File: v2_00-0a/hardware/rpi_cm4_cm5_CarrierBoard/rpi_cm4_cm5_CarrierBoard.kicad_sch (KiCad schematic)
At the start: 5 parts

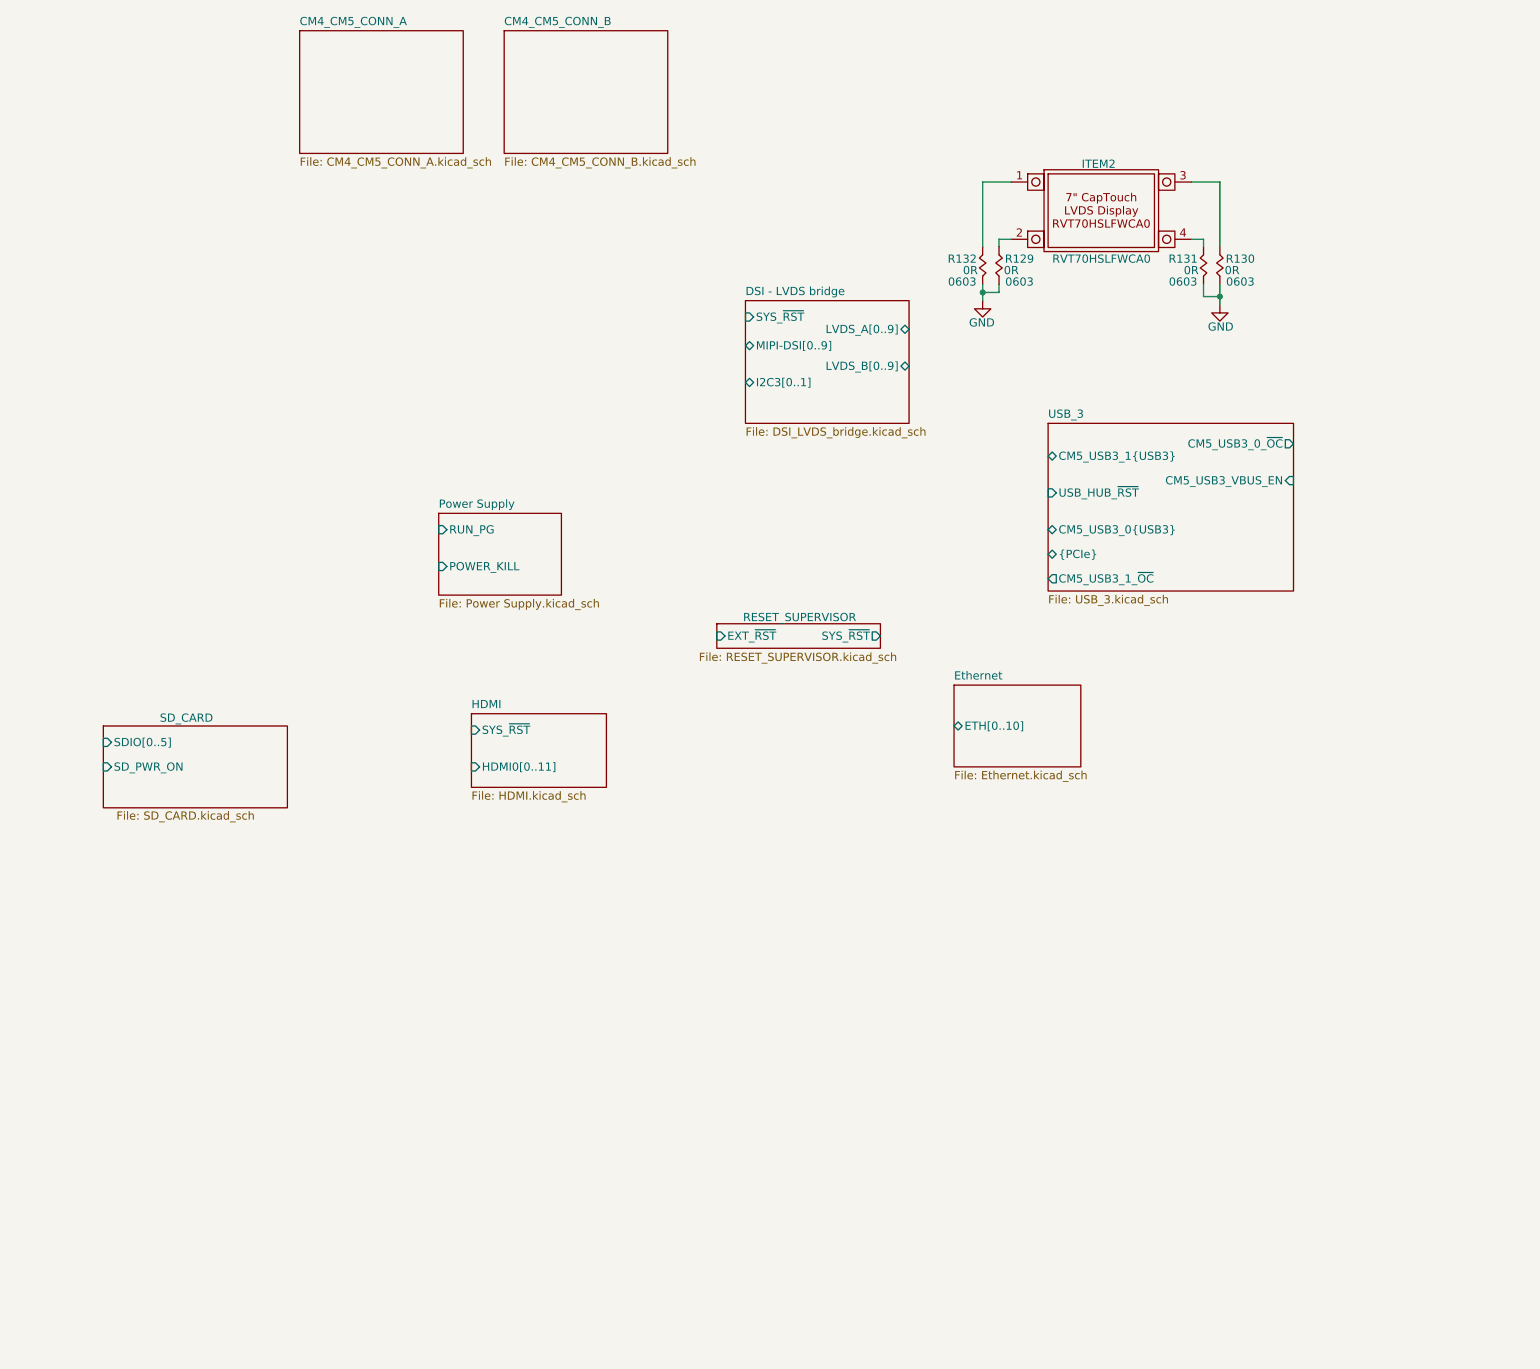
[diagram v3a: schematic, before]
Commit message: Add new page and update schematics
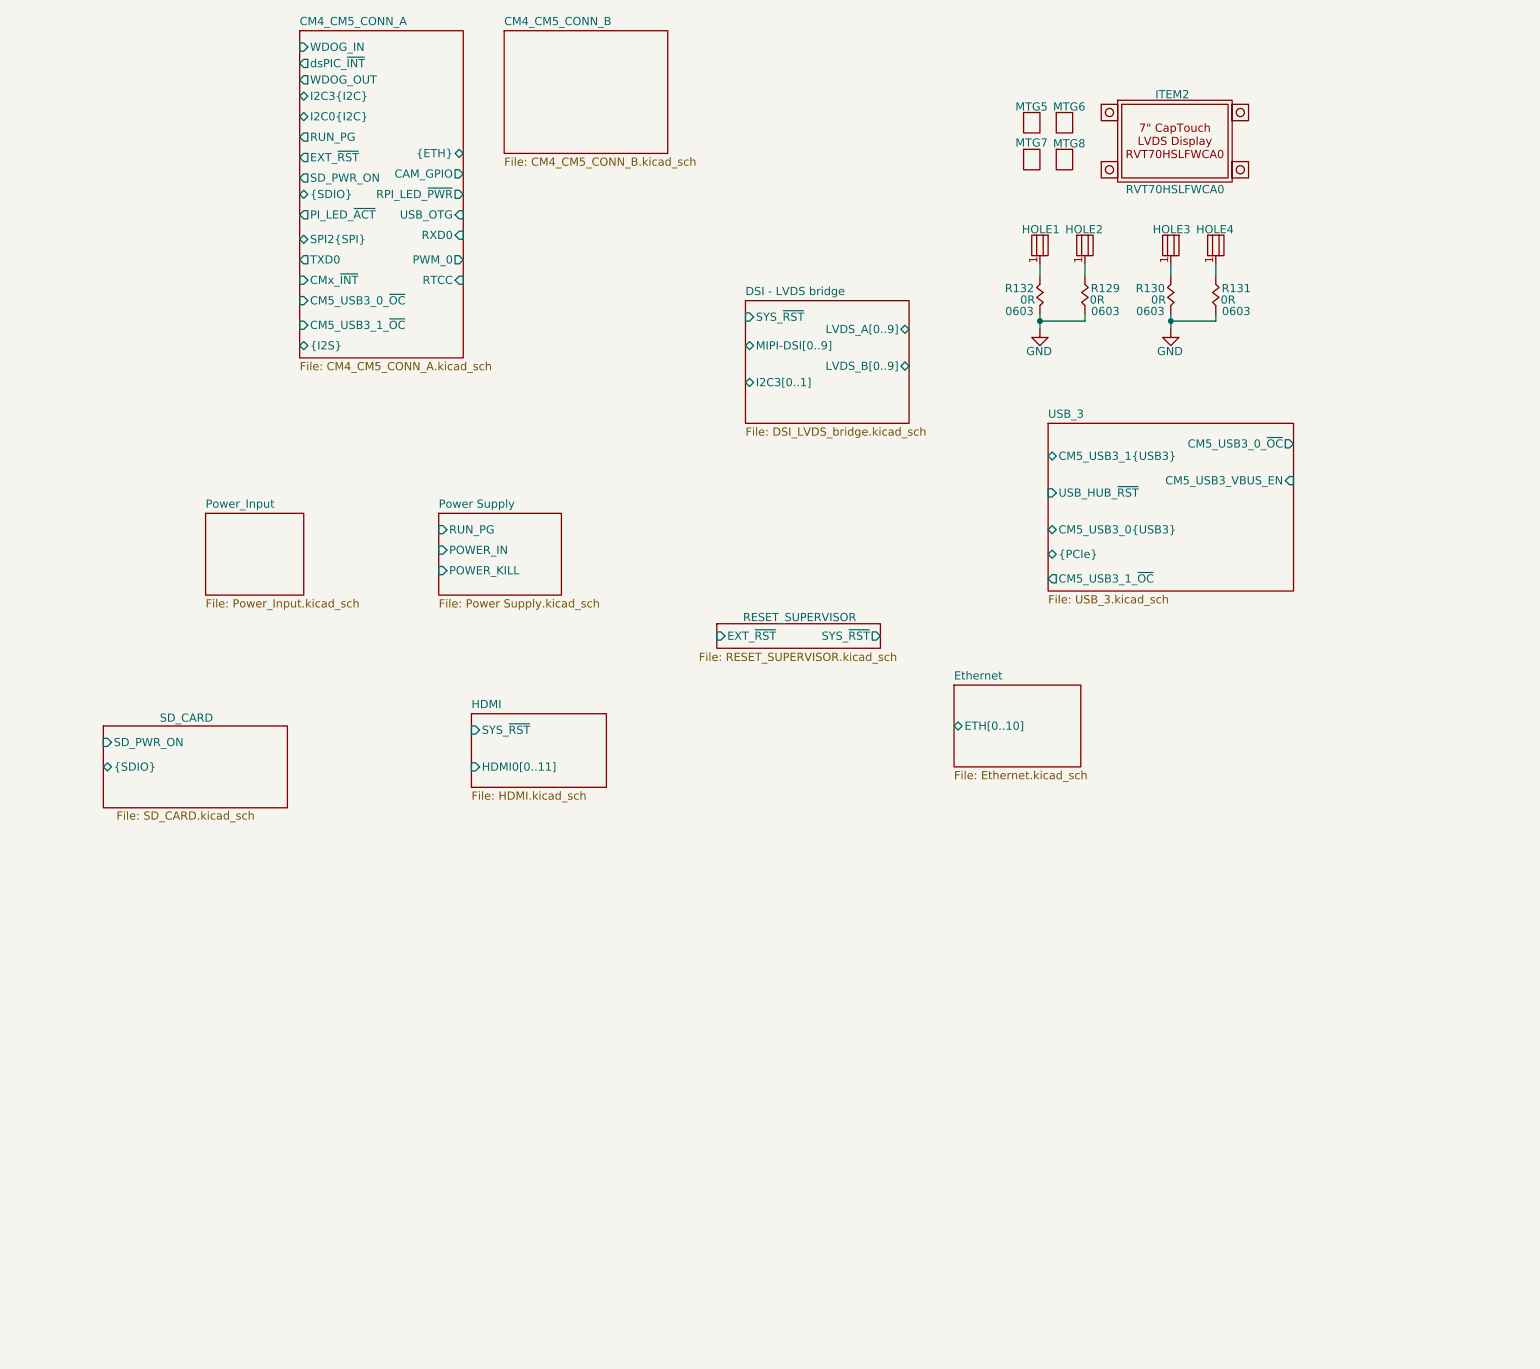
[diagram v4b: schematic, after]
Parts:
- added HOLE1, HOLE2, HOLE3, HOLE4: MTG_hole_cir_5mm_pad_3mm_drill, MTG_hole_cir_5mm_pad_3mm_drill, symbol KiCad_Lib_Symbols:MTG_hole_cir_5mm_pad_3mm_drill
- added MTG5, MTG6, MTG7, MTG8: M0504-25-AL-7, footprint:M0504-25-AL-7, symbol KicadCompDb:Miscellaneous/MISC_00004
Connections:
- net at R130.1: now also HOLE3.1; no longer ITEM2.3
- net at R132.1: now also HOLE1.1; no longer ITEM2.1
- net at R129.1: now also HOLE2.1; no longer ITEM2.2
- net at R131.1: now also HOLE4.1; no longer ITEM2.4
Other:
- added sheet Power_Input (Power_Input.kicad_sch)
- sheet CM4_CM5_CONN_A ports: added CAM_GPIO, CM5_USB3_0_~{OC}, CM5_USB3_1_~{OC}, CMx_~{INT}, EXT_~{RST}, I2C0{I2C}, I2C3{I2C}, PI_LED_~{ACT}, PWM_0, RPI_LED_~{PWR}, RTCC, RUN_PG, RXD0, SD_PWR_ON, SPI2{SPI}, TXD0, USB_OTG, WDOG_IN, WDOG_OUT, dsPIC_~{INT}, {ETH}, {I2S}, {SDIO}; removed none
- sheet Power Supply ports: added POWER_IN; removed none
- sheet SD_CARD ports: added {SDIO}; removed SDIO[0..5]
- moved on the sheet: R129, R132

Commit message: Add design notes (power table) and latest changes to power supply and power input
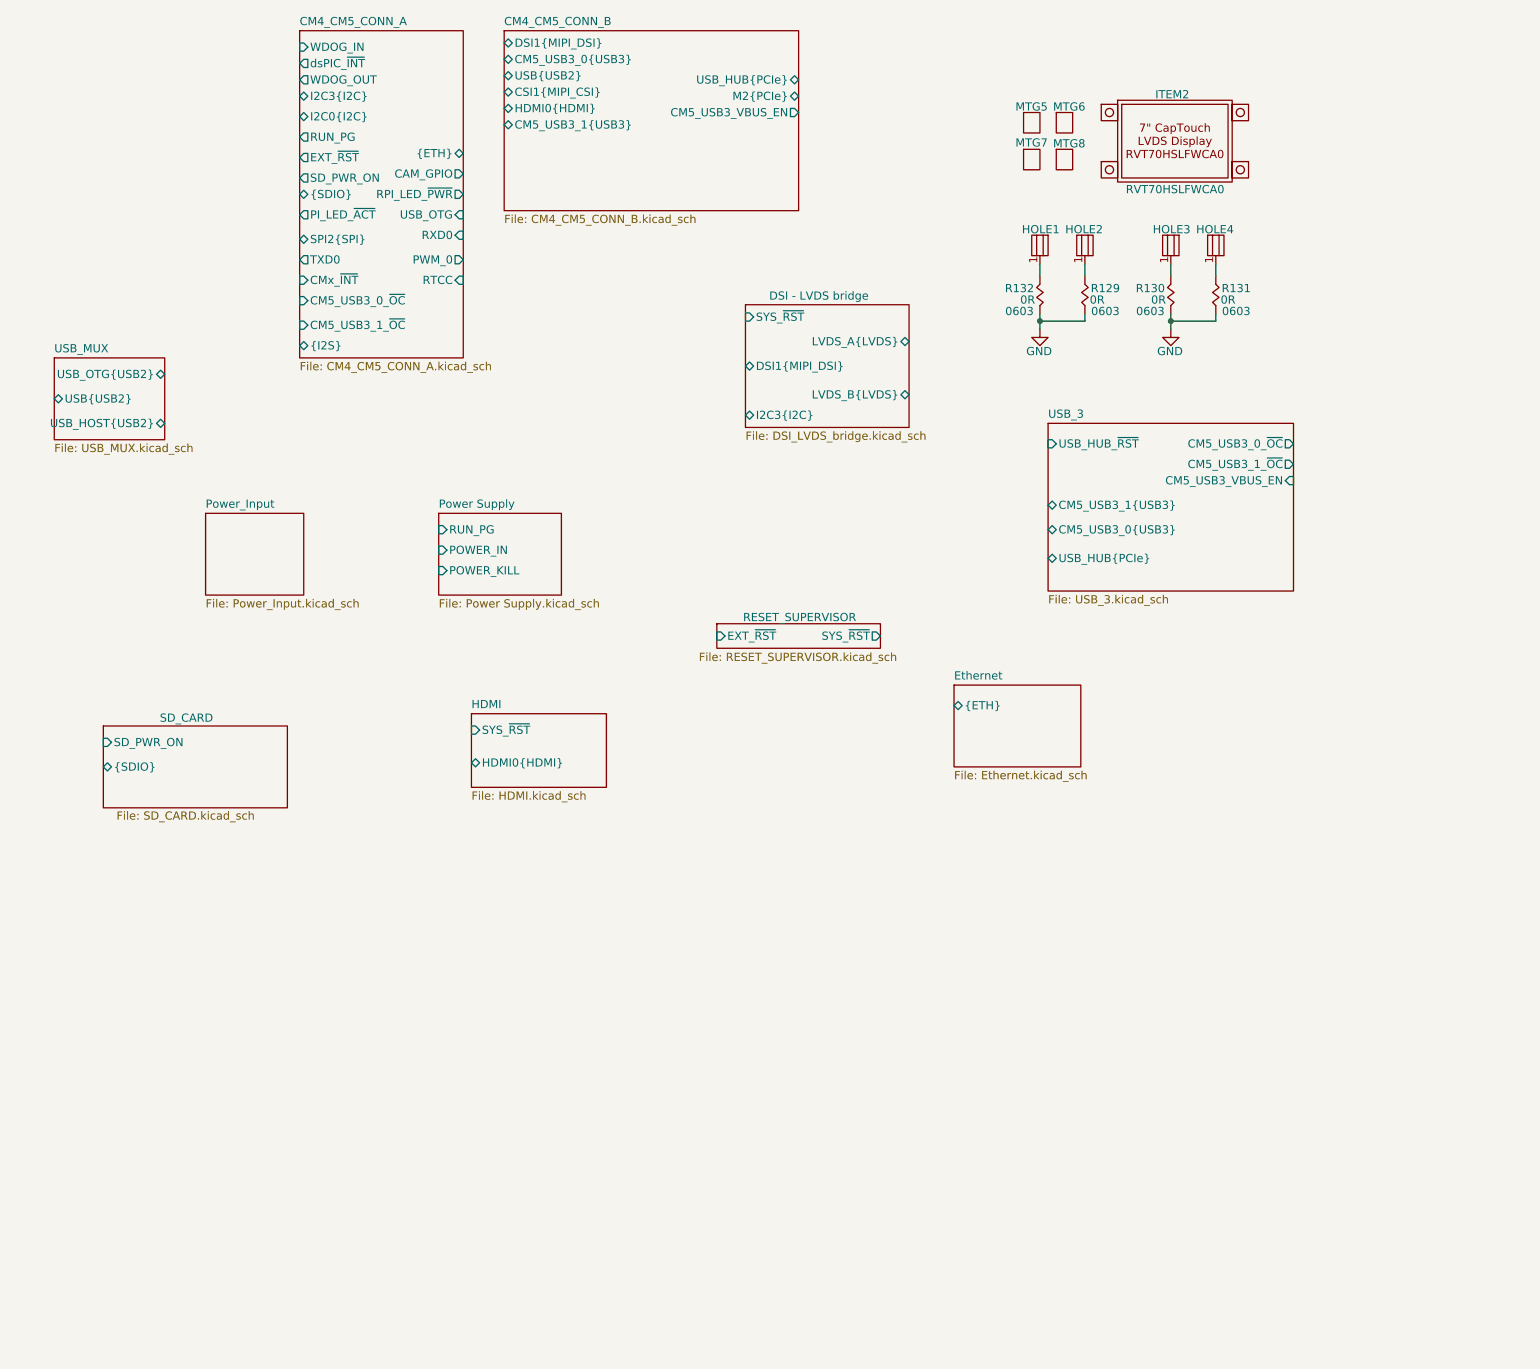
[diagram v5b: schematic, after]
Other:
- added sheet USB_MUX (USB_MUX.kicad_sch)
- sheet CM4_CM5_CONN_B ports: added CM5_USB3_0{USB3}, CM5_USB3_1{USB3}, CM5_USB3_VBUS_EN, CSI1{MIPI_CSI}, DSI1{MIPI_DSI}, HDMI0{HDMI}, M2{PCIe}, USB_HUB{PCIe}, USB{USB2}; removed none
- sheet DSI - LVDS bridge ports: added DSI1{MIPI_DSI}, I2C3{I2C}, LVDS_A{LVDS}, LVDS_B{LVDS}; removed I2C3[0..1], LVDS_A[0..9], LVDS_B[0..9], MIPI-DSI[0..9]
- sheet Ethernet ports: added {ETH}; removed ETH[0..10]
- sheet HDMI ports: added HDMI0{HDMI}; removed HDMI0[0..11]
- sheet USB_3 ports: added USB_HUB{PCIe}; removed {PCIe}
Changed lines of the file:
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@@
 		)
 		(pin "USB_HUB_~{RST}" input
-			(at 217.805 97.155 180)
+			(at 217.805 89.535 180)
 			(effects
 				(font
@@
 		)
 		(pin "CM5_USB3_1_~{OC}" output
-			(at 217.805 110.49 180)
-			(effects
-				(font
-					(size 1.27 1.27)
-				)
-				(justify left)
+			(at 255.905 92.71 0)
+			(effects
+				(font
+					(size 1.27 1.27)
+				)
+				(justify right)
 			)
 		)
@@
 		)
 		(pin "CM5_USB3_1{USB3}" bidirectional
-			(at 217.805 91.44 180)
-			(effects
-				(font
-					(size 1.27 1.27)
-				)
-				(justify left)
-			)
-		)
-		(pin "{PCIe}" bidirectional
-			(at 217.805 106.68 180)
+			(at 217.805 99.06 180)
+			(effects
+				(font
+					(size 1.27 1.27)
+				)
+				(justify left)
+			)
+		)
+		(pin "USB_HUB{PCIe}" bidirectional
+			(at 217.805 107.315 180)
 			(effects
 				(font
@@
 	(sheet
 		(at 133.35 25.4)
-		(size 25.4 19.05)
+		(size 45.72 27.94)
 		(exclude_from_sim no)
 		(in_bom yes)
@@
 		)
 		(property "Sheetfile" "CM4_CM5_CONN_B.kicad_sch"
-			(at 133.35 45.0346 0)
+			(at 133.35 53.9246 0)
 			(effects
 				(font
@@
 				)
 				(justify left top)
+			)
+		)
+		(pin "DSI1{MIPI_DSI}" bidirectional
+			(at 133.35 27.305 180)
+			(effects
+				(font
+					(size 1.27 1.27)
+				)
+				(justify left)
+			)
+		)
+		(pin "CM5_USB3_0{USB3}" bidirectional
+			(at 133.35 29.845 180)
+			(effects
+				(font
+					(size 1.27 1.27)
+				)
+				(justify left)
+			)
+		)
+		(pin "USB{USB2}" bidirectional
+			(at 133.35 32.385 180)
+			(effects
+				(font
+					(size 1.27 1.27)
+				)
+				(justify left)
+			)
+		)
+		(pin "CSI1{MIPI_CSI}" bidirectional
+			(at 133.35 34.925 180)
+			(effects
+				(font
+					(size 1.27 1.27)
+				)
+				(justify left)
+			)
+		)
+		(pin "HDMI0{HDMI}" bidirectional
+			(at 133.35 37.465 180)
+			(effects
+				(font
+					(size 1.27 1.27)
+				)
+				(justify left)
+			)
+		)
+		(pin "CM5_USB3_1{USB3}" bidirectional
+			(at 133.35 40.005 180)
+			(effects
+				(font
+					(size 1.27 1.27)
+				)
+				(justify left)
+			)
+		)
+		(pin "USB_HUB{PCIe}" bidirectional
+			(at 179.07 33.02 0)
+			(effects
+				(font
+					(size 1.27 1.27)
+				)
+				(justify right)
+			)
+		)
+		(pin "CM5_USB3_VBUS_EN" output
+			(at 179.07 38.1 0)
+			(effects
+				(font
+					(size 1.27 1.27)
+				)
+				(justify right)
+			)
+		)
+		(pin "M2{PCIe}" bidirectional
+			(at 179.07 35.56 0)
+			(effects
+				(font
+					(size 1.27 1.27)
+				)
+				(justify right)
 			)
 		)
@@
 				(path "/7dcdf741-90ca-4333-848c-806f4d64158e"
 					(page "10")
+				)
+			)
+		)
+	)
+	(sheet
+		(at 63.5 76.2)
+		(size 17.145 12.7)
+		(exclude_from_sim no)
+		(in_bom yes)
+		(on_board yes)
+		(dnp no)
+		(fields_autoplaced yes)
+		(stroke
+			(width 0.1524)
+			(type solid)
+		)
+		(fill
+			(color 0 0 0 0.0000)
+		)
+		(property "Sheetname" "USB_MUX"
+			(at 63.5 75.4884 0)
+			(effects
+				(font
+					(size 1.27 1.27)
+				)
+				(justify left bottom)
+			)
+		)
+		(property "Sheetfile" "USB_MUX.kicad_sch"
+			(at 63.5 89.4846 0)
+			(effects
+				(font
+					(size 1.27 1.27)
+				)
+				(justify left top)
+			)
+		)
+		(pin "USB{USB2}" bidirectional
+			(at 63.5 82.55 180)
+			(effects
+				(font
+					(size 1.27 1.27)
+				)
+				(justify left)
+			)
+		)
+		(pin "USB_OTG{USB2}" bidirectional
+			(at 80.645 78.74 0)
+			(effects
+				(font
+					(size 1.27 1.27)
+				)
+				(justify right)
+			)
+		)
+		(pin "USB_HOST{USB2}" bidirectional
+			(at 80.645 86.36 0)
+			(effects
+				(font
+					(size 1.27 1.27)
+				)
+				(justify right)
+			)
+		)
+		(instances
+			(project "rpi_cm4_cm5_CarrierBoard"
+				(path "/7dcdf741-90ca-4333-848c-806f4d64158e"
+					(page "12")
 				)
 			)
@@
 	)
 	(sheet
-		(at 170.815 67.31)
+		(at 170.815 67.945)
 		(size 25.4 19.05)
 		(exclude_from_sim no)
@@
 		(on_board yes)
 		(dnp no)
-		(fields_autoplaced yes)
 		(stroke
 			(width 0.1524)
@@
 		)
 		(property "Sheetname" "DSI - LVDS bridge"
-			(at 170.815 66.5984 0)
+			(at 174.498 67.31 0)
 			(effects
 				(font
@@
 		)
 		(property "Sheetfile" "DSI_LVDS_bridge.kicad_sch"
-			(at 170.815 86.9446 0)
+			(at 170.815 87.5796 0)
 			(effects
 				(font
@@
 			)
 		)
-		(pin "MIPI-DSI[0..9]" bidirectional
-			(at 170.815 74.295 180)
-			(effects
-				(font
-					(size 1.27 1.27)
-				)
-				(justify left)
-			)
-		)
-		(pin "I2C3[0..1]" bidirectional
-			(at 170.815 80.01 180)
-			(effects
-				(font
-					(size 1.27 1.27)
-				)
-				(justify left)
-			)
-		)
-		(pin "LVDS_A[0..9]" bidirectional
-			(at 196.215 71.755 0)
-			(effects
-				(font
-					(size 1.27 1.27)
-				)
-				(justify right)
-			)
-		)
-		(pin "LVDS_B[0..9]" bidirectional
-			(at 196.215 77.47 0)
+		(pin "DSI1{MIPI_DSI}" bidirectional
+			(at 170.815 77.47 180)
+			(effects
+				(font
+					(size 1.27 1.27)
+				)
+				(justify left)
+			)
+		)
+		(pin "LVDS_A{LVDS}" bidirectional
+			(at 196.215 73.66 0)
+			(effects
+				(font
+					(size 1.27 1.27)
+				)
+				(justify right)
+			)
+		)
+		(pin "I2C3{I2C}" bidirectional
+			(at 170.815 85.09 180)
+			(effects
+				(font
+					(size 1.27 1.27)
+				)
+				(justify left)
+			)
+		)
+		(pin "LVDS_B{LVDS}" bidirectional
+			(at 196.215 81.915 0)
 			(effects
 				(font
@@
 			)
 		)
-		(pin "HDMI0[0..11]" input
-			(at 128.27 139.7 180)
+		(pin "HDMI0{HDMI}" bidirectional
+			(at 128.27 139.065 180)
 			(effects
 				(font
@@
 			)
 		)
-		(pin "ETH[0..10]" bidirectional
-			(at 203.2 133.35 180)
-			(effects
-				(font
+		(pin "{ETH}" bidirectional
+			(at 203.2 130.175 180)
+			(effects
+				(font

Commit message: Add TFT schematic pages (power + connector)
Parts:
- removed HOLE1, HOLE2, HOLE3, HOLE4: MTG_hole_cir_5mm_pad_3mm_drill, MTG_hole_cir_5mm_pad_3mm_drill, symbol KiCad_Lib_Symbols:MTG_hole_cir_5mm_pad_3mm_drill
- removed ITEM2: RVT70HSLFWCA0, footprint:RVT70HSLFWCA0, symbol KicadCompDb:Miscellaneous/MISC_00003
- removed MTG5, MTG6, MTG7, MTG8: M0504-25-AL-7, footprint:M0504-25-AL-7, symbol KicadCompDb:Miscellaneous/MISC_00004
- removed R129, R130, R131, R132: 0R, footprint:RES_0603, symbol KicadCompDb:Resistors/RES_SMT_00021
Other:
- added sheet TFT_CONN (TFT_CONN.kicad_sch)
- added sheet TFT_POWER (TFT_POWER.kicad_sch)

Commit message: Update schematic
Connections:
- no-connect marks 0 -> 1
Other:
- sheet TFT_POWER ports: added BL_PWM, SYS_~{RST}, TFT_-6V, TFT_18V, TFT_3V8, TFT_9V6, TFT_LED+, TFT_LED-, TFT_STBYB, TFT_VDD, TFT_~{RST}; removed none
